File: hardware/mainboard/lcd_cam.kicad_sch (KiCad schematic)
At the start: 48 parts, among them U19 ADP5070ACPZ, U20 CAT4106HV4

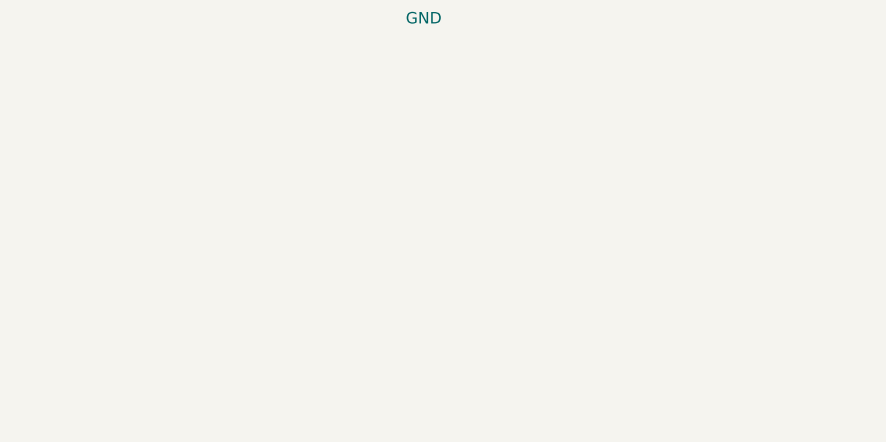
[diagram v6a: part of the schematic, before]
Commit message: Mechanical updates; add cam clk connectors
Signed-off-by: gatecat <gatecat@ds0.me>
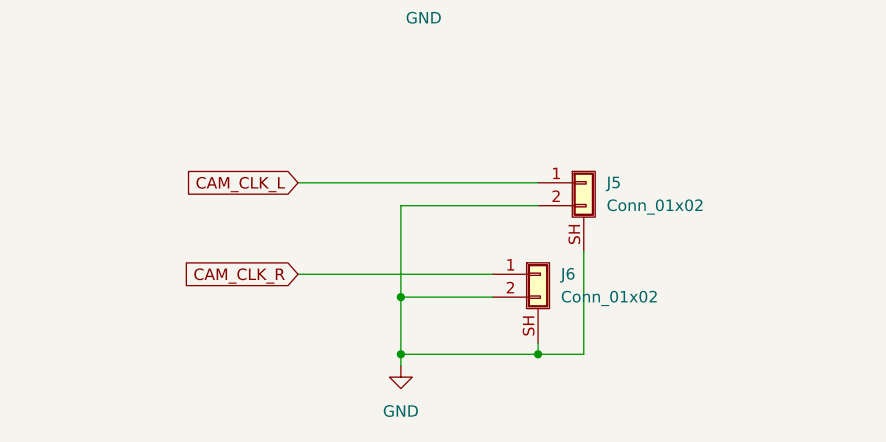
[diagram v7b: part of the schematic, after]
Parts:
- added J5, J6: Conn_01x02, meowality:TE-292227-2, symbol Connector_Generic_Shielded:Conn_01x02_Shielded
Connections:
- net GND: now also J5.2 (Pin_2), J5.SH (Shield), J6.2 (Pin_2), J6.SH (Shield)
- new net CAM_CLK_L: J5.1 (Pin_1)
- new net CAM_CLK_R: J6.1 (Pin_1)
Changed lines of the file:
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@@
   (junction (at 335.28 97.79) (diameter 0) (color 0 0 0 0)
   )
+  (junction (at 147.32 260.35) (diameter 0) (color 0 0 0 0)
+  )
   (junction (at 251.46 201.93) (diameter 0) (color 0 0 0 0)
   )
@@
   (junction (at 342.9 186.69) (diameter 0) (color 0 0 0 0)
   )
+  (junction (at 132.08 254) (diameter 0) (color 0 0 0 0)
+  )
   (junction (at 210.82 246.38) (diameter 0) (color 0 0 0 0)
   )
   (junction (at 245.11 120.65) (diameter 0) (color 0 0 0 0)
+  )
+  (junction (at 132.08 260.35) (diameter 0) (color 0 0 0 0)
   )
   (junction (at 311.15 171.45) (diameter 0) (color 0 0 0 0)
@@
     (stroke (width 0) (type default) (color 0 0 0 0))
   )
+  (wire (pts (xy 147.32 243.84) (xy 132.08 243.84))
+    (stroke (width 0) (type default) (color 0 0 0 0))
+  )
   (wire (pts (xy 311.15 123.19) (xy 313.69 123.19))
     (stroke (width 0) (type default) (color 0 0 0 0))
@@
     (stroke (width 0) (type default) (color 0 0 0 0))
   )
+  (wire (pts (xy 152.4 260.35) (xy 147.32 260.35))
+    (stroke (width 0) (type default) (color 0 0 0 0))
+  )
   (wire (pts (xy 257.81 215.9) (xy 261.62 215.9))
     (stroke (width 0) (type default) (color 0 0 0 0))
@@
     (stroke (width 0) (type default) (color 0 0 0 0))
   )
+  (wire (pts (xy 132.08 260.35) (xy 147.32 260.35))
+    (stroke (width 0) (type default) (color 0 0 0 0))
+  )
   (wire (pts (xy 176.53 105.41) (xy 176.53 110.49))
     (stroke (width 0) (type default) (color 0 0 0 0))
@@
     (stroke (width 0) (type default) (color 0 0 0 0))
   )
+  (wire (pts (xy 152.4 248.92) (xy 152.4 260.35))
+    (stroke (width 0) (type default) (color 0 0 0 0))
+  )
   (wire (pts (xy 198.12 107.95) (xy 198.12 105.41))
     (stroke (width 0) (type default) (color 0 0 0 0))
@@
     (stroke (width 0) (type default) (color 0 0 0 0))
   )
+  (wire (pts (xy 147.32 260.35) (xy 147.32 259.08))
+    (stroke (width 0) (type default) (color 0 0 0 0))
+  )
   (wire (pts (xy 185.42 105.41) (xy 198.12 105.41))
     (stroke (width 0) (type default) (color 0 0 0 0))
@@
     (stroke (width 0) (type default) (color 0 0 0 0))
   )
+  (wire (pts (xy 132.08 243.84) (xy 132.08 254))
+    (stroke (width 0) (type default) (color 0 0 0 0))
+  )
   (wire (pts (xy 354.33 173.99) (xy 359.41 173.99))
     (stroke (width 0) (type default) (color 0 0 0 0))
@@
     (stroke (width 0) (type default) (color 0 0 0 0))
   )
+  (wire (pts (xy 120.65 241.3) (xy 147.32 241.3))
+    (stroke (width 0) (type default) (color 0 0 0 0))
+  )
   (wire (pts (xy 124.46 34.29) (xy 137.16 34.29))
     (stroke (width 0) (type default) (color 0 0 0 0))
@@
     (stroke (width 0) (type default) (color 0 0 0 0))
   )
+  (wire (pts (xy 132.08 254) (xy 142.24 254))
+    (stroke (width 0) (type default) (color 0 0 0 0))
+  )
   (wire (pts (xy 386.08 135.89) (xy 356.87 135.89))
     (stroke (width 0) (type default) (color 0 0 0 0))
@@
     (stroke (width 0) (type default) (color 0 0 0 0))
   )
+  (wire (pts (xy 132.08 254) (xy 132.08 260.35))
+    (stroke (width 0) (type default) (color 0 0 0 0))
+  )
   (wire (pts (xy 124.46 46.99) (xy 137.16 46.99))
     (stroke (width 0) (type default) (color 0 0 0 0))
@@
     (stroke (width 0) (type default) (color 0 0 0 0))
   )
+  (wire (pts (xy 120.65 251.46) (xy 142.24 251.46))
+    (stroke (width 0) (type default) (color 0 0 0 0))
+  )
   (wire (pts (xy 297.18 36.83) (xy 313.69 36.83))
     (stroke (width 0) (type default) (color 0 0 0 0))
@@
   )
   (wire (pts (xy 134.62 215.9) (xy 134.62 218.44))
+    (stroke (width 0) (type default) (color 0 0 0 0))
+  )
+  (wire (pts (xy 132.08 260.35) (xy 132.08 261.62))
     (stroke (width 0) (type default) (color 0 0 0 0))
   )
@@
     )
   )
+  (global_label "CAM_CLK_R" (shape input) (at 120.65 251.46 180) (fields_autoplaced)
+    (effects (font (size 1.27 1.27)) (justify right))
+    (property "Intersheet References" "${INTERSHEET_REFS}" (id 0) (at 107.6536 251.3806 0)
+      (effects (font (size 1.27 1.27)) (justify right) hide)
+    )
+  )
   (global_label "DSI0B_D3-" (shape input) (at 298.45 41.91 180) (fields_autoplaced)
     (effects (font (size 1.27 1.27)) (justify right))
@@
     (effects (font (size 1.27 1.27)) (justify right))
     (property "Intersheet References" "${INTERSHEET_REFS}" (id 0) (at 114.0036 186.6106 0)
+      (effects (font (size 1.27 1.27)) (justify right) hide)
+    )
+  )
+  (global_label "CAM_CLK_L" (shape input) (at 120.65 241.3 180) (fields_autoplaced)
+    (effects (font (size 1.27 1.27)) (justify right))
+    (property "Intersheet References" "${INTERSHEET_REFS}" (id 0) (at 107.8955 241.3794 0)
       (effects (font (size 1.27 1.27)) (justify right) hide)
     )
@@
     (pin "1")
     (pin "2")
+  )
+  (symbol (lib_id "power:GND") (at 132.08 261.62 0) (unit 1)
+    (in_bom yes) (on_board yes) (fields_autoplaced)
+    (property "Reference" "#PWR015" (id 0) (at 132.08 267.97 0)
+      (effects (font (size 1.27 1.27)) hide)
+    )
+    (property "Value" "GND" (id 1) (at 132.08 266.7 0))
+    (property "Footprint" "" (id 2) (at 132.08 261.62 0)
+      (effects (font (size 1.27 1.27)) hide)
+    )
+    (property "Datasheet" "" (id 3) (at 132.08 261.62 0)
+      (effects (font (size 1.27 1.27)) hide)
+    )
+    (pin "1")
   )
   (symbol (lib_id "Connector:TestPoint") (at 370.84 118.11 270) (unit 1)
@@
     (pin "2")
   )
+  (symbol (lib_id "Connector_Generic_Shielded:Conn_01x02_Shielded") (at 152.4 241.3 0) (unit 1)
+    (in_bom yes) (on_board yes) (fields_autoplaced)
+    (property "Reference" "J5" (id 0) (at 154.94 241.2999 0)
+      (effects (font (size 1.27 1.27)) (justify left))
+    )
+    (property "Value" "Conn_01x02" (id 1) (at 154.94 243.8399 0)
+      (effects (font (size 1.27 1.27)) (justify left))
+    )
+    (property "Footprint" "meowality:TE-292227-2" (id 2) (at 152.4 241.3 0)
+      (effects (font (size 1.27 1.27)) hide)
+    )
+    (property "Datasheet" "~" (id 3) (at 152.4 241.3 0)
+      (effects (font (size 1.27 1.27)) hide)
+    )
+    (pin "1")
+    (pin "2")
+    (pin "SH")
+  )
   (symbol (lib_id "Device:R_Small") (at 210.82 240.03 0) (unit 1)
     (in_bom yes) (on_board yes) (fields_autoplaced)
@@
     (pin "2")
   )
+  (symbol (lib_id "Connector_Generic_Shielded:Conn_01x02_Shielded") (at 147.32 251.46 0) (unit 1)
+    (in_bom yes) (on_board yes) (fields_autoplaced)
+    (property "Reference" "J6" (id 0) (at 149.86 251.4599 0)
+      (effects (font (size 1.27 1.27)) (justify left))
+    )
+    (property "Value" "Conn_01x02" (id 1) (at 149.86 253.9999 0)
+      (effects (font (size 1.27 1.27)) (justify left))
+    )
+    (property "Footprint" "meowality:TE-292227-2" (id 2) (at 147.32 251.46 0)
+      (effects (font (size 1.27 1.27)) hide)
+    )
+    (property "Datasheet" "~" (id 3) (at 147.32 251.46 0)
+      (effects (font (size 1.27 1.27)) hide)
+    )
+    (pin "1")
+    (pin "2")
+    (pin "SH")
+  )
   (symbol (lib_id "Device:D_Schottky_Small") (at 247.65 138.43 0) (unit 1)

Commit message: Rework LCD PWM setup
Signed-off-by: gatecat <gatecat@ds0.me>
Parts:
- added C79: 1µ, Capacitor_SMD:C_0603_1608Metric, symbol Device:C_Small
- added R100, R26, R99: 10k, Resistor_SMD:R_0402_1005Metric, symbol Device:R_Small
- added R98: 33k, Resistor_SMD:R_0402_1005Metric, symbol Device:R_Small
- added U18: MCP6566R, Package_TO_SOT_SMD:SOT-23-5, symbol Comparator:MCP6566R
- added U22: 74AHC1G08, Package_TO_SOT_SMD:SOT-23-5, symbol 74xGxx:74AHC1G08
- R94: value 10k -> 47k
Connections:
- net +3V3PL: now also R98.2, U18.2 (V+), U22.5 (VCC)
- net GND: now also C79.2, R100.1, R26.1, R99.1, U18.5 (V-), U22.3 (GND); no longer R94.2
- removed net LCD_LEDPWM: LCD1.48 (LEDPWM), R94.1, U20.7 (EN/PWM)
- new net: C79.1, R94.2, U18.4 (-)
- new net: U18.1, U22.1
- new net: R98.1, R99.2, U18.3 (+)
- new net BL_PWM: R26.2, R94.1, U22.2
- new net PWM_GATE: R100.2, U20.7 (EN/PWM), U22.4
- no-connect marks 7 -> 8
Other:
- note added: "Protects the LEDs from PWM > 23%"
- note removed: "TODO: PWM gate, safety watchdog?"
- moved on the sheet: J5, J6
